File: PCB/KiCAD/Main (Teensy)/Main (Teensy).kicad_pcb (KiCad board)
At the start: 2 copper layers, 150 x 137.2 mm, 158 parts, among them J1 Conn_02x03_Odd_Even, J10 Conn_01x04, J2 Conn_01x02, J3 Conn_01x04, J4 Conn_01x04, J5 Conn_01x02, J6 Conn_01x06, J7 Conn_01x04, J8 Conn_01x02, J9 Conn_01x02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

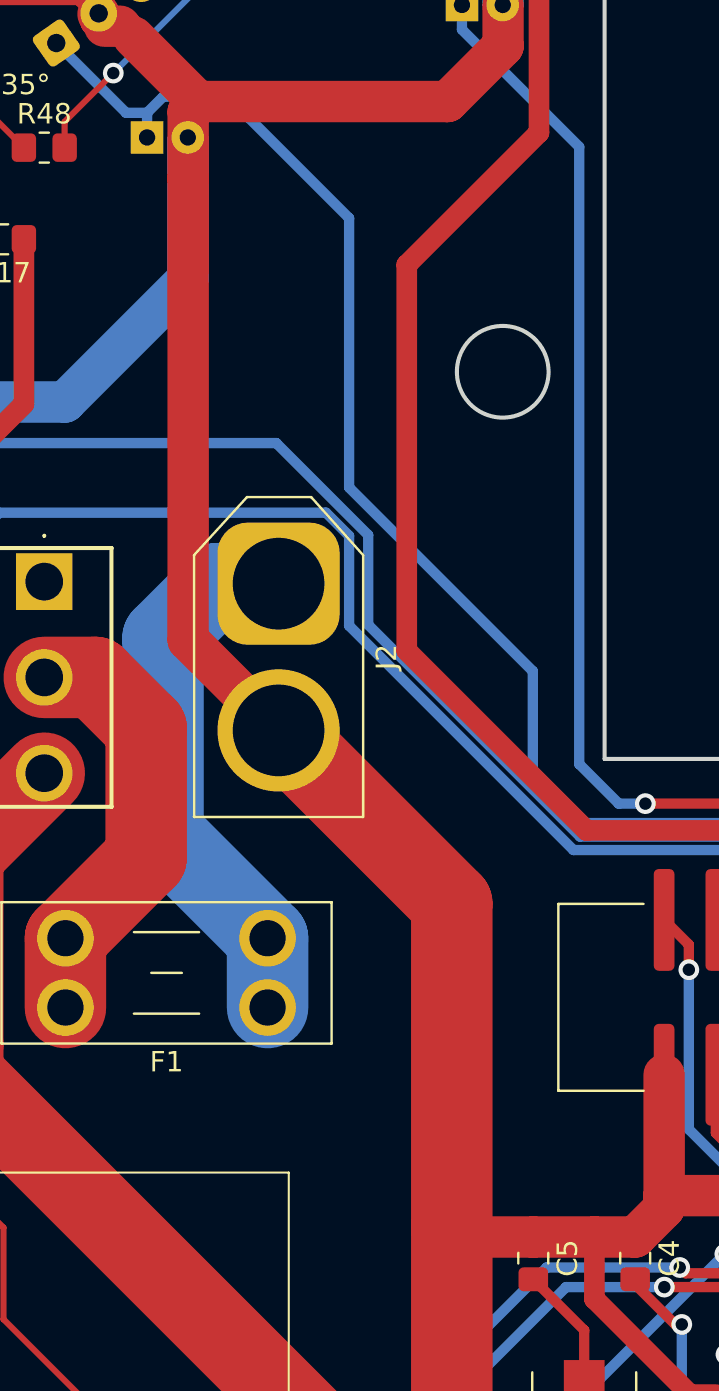
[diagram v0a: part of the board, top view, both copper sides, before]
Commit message: Battery XT60 was reversed
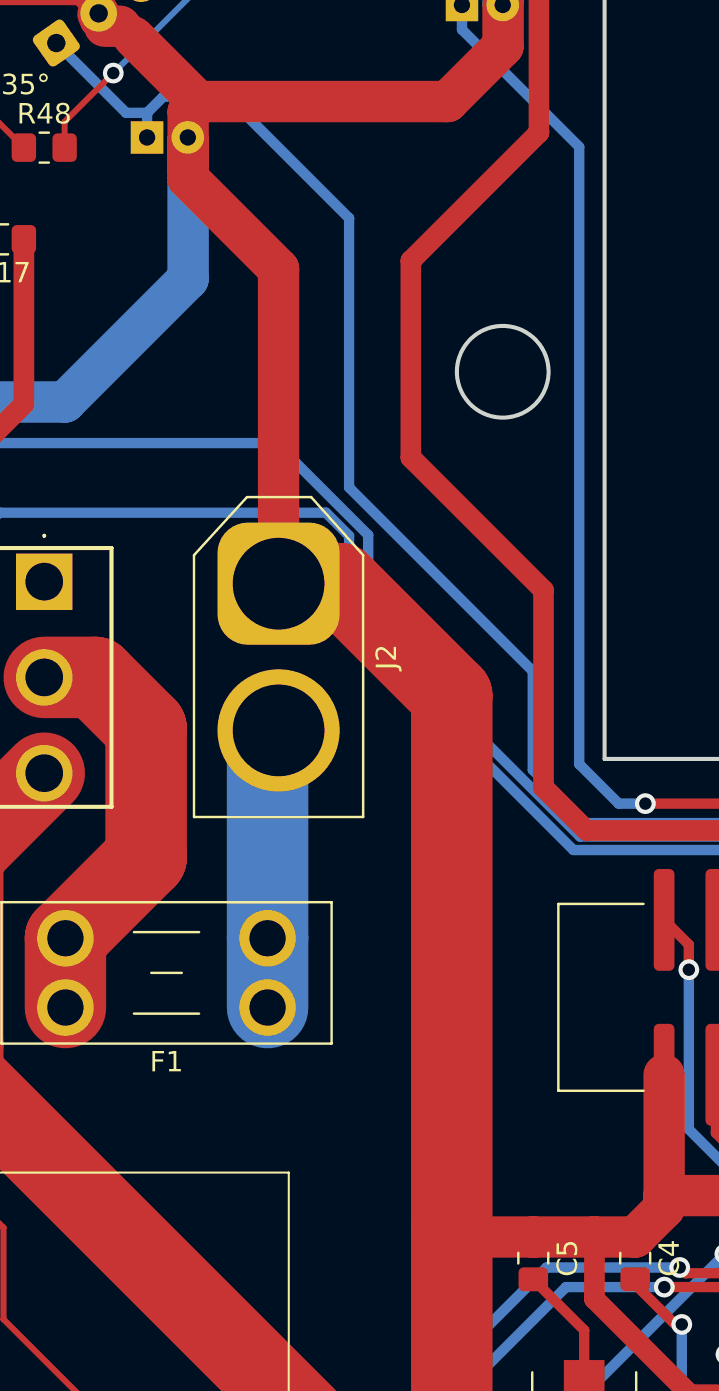
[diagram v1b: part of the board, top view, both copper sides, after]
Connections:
- F1 pad 1: Net-(J2-Pin_1) -> Net-(J2-Pin_2)
- J2 pad 1: Net-(J2-Pin_1) -> Earth
- J2 pad 2: Earth -> Net-(J2-Pin_2)
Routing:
- net Net-(J2-Pin_1): track 27.0 -> 0.00 mm
- net Net-(J2-Pin_2): track 0.00 -> 13.8 mm
- net Earth: track 1209.6 -> 1211.3 mm
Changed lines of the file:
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@@
 	(net 86 "Net-(IR23-OUT)")
 	(net 87 "Net-(IR24-OUT)")
-	(net 88 "Net-(J2-Pin_1)")
+	(net 88 "Net-(J2-Pin_2)")
 	(net 89 "Net-(S1-COM)")
 	(net 90 "unconnected-(S1-NC-Pad1)")
@@
 			(remove_unused_layers no)
 			(roundrect_rratio 0.25)
-			(net 88 "Net-(J2-Pin_1)")
+			(net 6 "Earth")
 			(pinfunction "Pin_1")
 			(pintype "passive")
@@
 			(layers "*.Cu" "*.Mask")
 			(remove_unused_layers no)
-			(net 6 "Earth")
+			(net 88 "Net-(J2-Pin_2)")
 			(pinfunction "Pin_2")
 			(pintype "passive")
@@
 			(layers "*.Cu" "*.Mask")
 			(remove_unused_layers no)
-			(net 88 "Net-(J2-Pin_1)")
+			(net 88 "Net-(J2-Pin_2)")
 			(pintype "passive")
 		)
@@
 			(layers "*.Cu" "*.Mask")
 			(remove_unused_layers no)
-			(net 88 "Net-(J2-Pin_1)")
+			(net 88 "Net-(J2-Pin_2)")
 			(pintype "passive")
 		)
@@
 	)
 	(segment
-		(start 35 51)
-		(end 33 51)
-		(width 1.016)
-		(layer "F.Cu")
-		(net 1)
-	)
-	(segment
-		(start -7.5818 -16.4899)
-		(end -15.8888 -16.4899)
+		(start -24.508 -44.4507)
+		(end -18.2218 -50.7369)
 		(width 1.016)
 		(layer "F.Cu")
@@
 	)
 	(segment
-		(start -15.8888 -16.4899)
-		(end -24.7091 -25.3102)
+		(start 35 51)
+		(end 33 51)
 		(width 1.016)
 		(layer "F.Cu")
@@
 	)
 	(segment
-		(start -24.7091 -25.3102)
-		(end -24.7091 -44.2496)
-		(width 1.016)
-		(layer "F.Cu")
-		(net 1)
-	)
-	(segment
 		(start 23.2029 -24.0388)
 		(end 22.5484 -24.6933)
@@
 	)
 	(segment
-		(start 6.9897 12.0648)
-		(end 3.8862 12.0648)
+		(start -18 -18.6011)
+		(end -18 -28.281578)
 		(width 1.016)
 		(layer "F.Cu")
@@
 	)
 	(segment
-		(start -24.7091 -44.2496)
-		(end -18.2218 -50.7369)
+		(start 6.9897 12.0648)
+		(end 3.8862 12.0648)
 		(width 1.016)
 		(layer "F.Cu")
@@
 	)
 	(segment
+		(start -5.8269 -5.6731)
+		(end -5.8269 -14.735)
+		(width 1.016)
+		(layer "F.Cu")
+		(net 1)
+	)
+	(segment
 		(start -35.31 24.576)
 		(end -35.31 26.0006)
@@
 	)
 	(segment
-		(start -3 40.0976)
-		(end -3 40)
+		(start -18.2218 -50.7369)
+		(end -18.2218 -59.5)
 		(width 1.016)
 		(layer "F.Cu")
@@
 	)
 	(segment
-		(start 1.4842 48.8458)
-		(end 1.3694 48.9606)
+		(start -3 40.0976)
+		(end -3 40)
 		(width 1.016)
 		(layer "F.Cu")
@@
 	)
 	(segment
-		(start -18.2218 -50.7369)
-		(end -18.2218 -59.5)
+		(start 1.4842 48.8458)
+		(end 1.3694 48.9606)
 		(width 1.016)
 		(layer "F.Cu")
@@
 	)
 	(segment
-		(start -5.8269 -5.6731)
-		(end -5.8269 -14.735)
-		(width 1.016)
-		(layer "F.Cu")
-		(net 1)
-	)
-	(segment
 		(start 9.241 21.5082)
 		(end 7.9357 20.2029)
@@
 	)
 	(segment
+		(start -15.8888 -16.4899)
+		(end -18 -18.6011)
+		(width 1.016)
+		(layer "F.Cu")
+		(net 1)
+	)
+	(segment
 		(start -52.5981 13.3569)
 		(end -58.4751 13.3569)
@@
 	)
 	(segment
+		(start -18 -28.281578)
+		(end -24.508 -34.789578)
+		(width 1.016)
+		(layer "F.Cu")
+		(net 1)
+	)
+	(segment
 		(start 13.9625 0.5375)
 		(end 13.2804 0.5375)
@@
 	)
 	(segment
-		(start -5.8269 -14.735)
-		(end -7.5818 -16.4899)
+		(start -7.5818 -16.4899)
+		(end -15.8888 -16.4899)
 		(width 1.016)
 		(layer "F.Cu")
@@
 	)
 	(segment
+		(start -24.508 -34.789578)
+		(end -24.508 -44.4507)
+		(width 1.016)
+		(layer "F.Cu")
+		(net 1)
+	)
+	(segment
 		(start -28.4388 51.3397)
 		(end -32.079 47.6995)
@@
 	)
 	(segment
+		(start -5.8269 -14.735)
+		(end -7.5818 -16.4899)
+		(width 1.016)
+		(layer "F.Cu")
+		(net 1)
+	)
+	(segment
 		(start 1.4842 43.2165)
 		(end 6.1764 43.2165)
@@
 	)
 	(segment
-		(start -35.4391 -51.7547)
-		(end -35.4391 -48.4823)
-		(width 2.032)
-		(layer "F.Cu")
-		(net 6)
-	)
-	(segment
 		(start 0.1 57.9)
 		(end 0.1 56.41)
@@
 	)
 	(segment
+		(start -35.4391 -48.4823)
+		(end -31 -44.0432)
+		(width 2.032)
+		(layer "F.Cu")
+		(net 6)
+	)
+	(segment
 		(start -5.5 47.5)
 		(end -2.016 47.5)
@@
 	)
 	(segment
+		(start -28 -28.6)
+		(end -31 -28.6)
+		(width 4)
+		(layer "F.Cu")
+		(net 6)
+	)
+	(segment
 		(start -27.001583 55.5)
 		(end -24.3561 55.5)
@@
 	)
 	(segment
+		(start -34.933 -52.2608)
+		(end -35.4391 -51.7547)
+		(width 2.032)
+		(layer "F.Cu")
+		(net 6)
+	)
+	(segment
 		(start -13.5 3.4625)
 		(end -15.5 3.4625)
@@
 	)
 	(segment
-		(start 50.95 -33.0051)
-		(end 48.516 -35.4391)
-		(width 2.032)
+		(start -22.5 -23.1)
+		(end -28 -28.6)
+		(width 4)
 		(layer "F.Cu")
 		(net 6)
 	)
 	(segment
-		(start -22.5 3)
-		(end -22.5 -12.9)
-		(width 4)
+		(start 50.95 -33.0051)
+		(end 48.516 -35.4391)
+		(width 2.032)
 		(layer "F.Cu")
 		(net 6)
@@
 	)
 	(segment
-		(start -35.4389 -25.8389)
-		(end -31 -21.4)
-		(width 2.032)
-		(layer "F.Cu")
-		(net 6)
-	)
-	(segment
 		(start 51 -25.5)
 		(end 51 -29.95)
@@
 	)
 	(segment
+		(start -31 -44.0432)
+		(end -31 -28.6)
+		(width 2.032)
+		(layer "F.Cu")
+		(net 6)
+	)
+	(segment
 		(start 67.059228 28.886264)
 		(end 66.44386 28.886264)
@@
 	)
 	(segment
+		(start -22.5 3)
+		(end -22.5 -23.1)
+		(width 4)
+		(layer "F.Cu")
+		(net 6)
+	)
+	(segment
 		(start -39.8632 -56.2847)
 		(end -39.8632 -56.5544)
@@
 	)
 	(segment
-		(start -35.4389 -48.4821)
-		(end -35.4389 -25.8389)
-		(width 2.032)
-		(layer "F.Cu")
-		(net 6)
-	)
-	(segment
-		(start -34.933 -52.2608)
-		(end -35.4391 -51.7547)
-		(width 2.032)
-		(layer "F.Cu")
-		(net 6)
-	)
-	(segment
-		(start -22.5 -12.9)
-		(end -31 -21.4)
-		(width 4)
-		(layer "F.Cu")
-		(net 6)
-	)
-	(segment
 		(start 18.3803 -25.6197)
 		(end 18.3803 -27.3803)
@@
 	)
 	(segment
+		(start -35.4391 -51.7547)
+		(end -35.4391 -48.4823)
+		(width 2.032)
+		(layer "F.Cu")
+		(net 6)
+	)
+	(segment
 		(start -37.5 22)
 		(end -39.639526 22)
@@
 	)
 	(segment
-		(start -35.4391 -48.4823)
-		(end -35.4389 -48.4821)
-		(width 2.032)
-		(layer "F.Cu")
-		(net 6)
-	)
-	(segment
 		(start -67.843699 26.992383)
 		(end -64.335423 26.992383)
@@
 	)
 	(segment
-		(start -36.6716 -25.9284)
-		(end -34 -28.6)
-		(width 4)
-		(layer "B.Cu")
-		(net 88)
-	)
-	(segment
-		(start -34 -28.6)
-		(end -31 -28.6)
-		(width 4)
-		(layer "B.Cu")
-		(net 88)
-	)
-	(segment
-		(start -36.6716 -16.3316)
-		(end -36.6716 -25.9284)
+		(start -31.54 -11.2)
+		(end -31.54 -20.86)
 		(width 4)
 		(layer "B.Cu")
@@
 	)
 	(segment
-		(start -31.54 -11.2)
-		(end -36.6716 -16.3316)
+		(start -31.54 -20.86)
+		(end -31 -21.4)
 		(width 4)
 		(layer "B.Cu")
